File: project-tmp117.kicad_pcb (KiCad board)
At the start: 2 copper layers, 17 parts, among them J1 Conn_01x01_Pin, J2 Conn_01x01_Pin, J3 Conn_01x01_Pin, J4 Conn_01x01_Pin, J5 Conn_01x01_Pin, J7 SM04B-SRSS-TB(LF)(SN), J8 SM04B-SRSS-TB(LF)(SN), U1 TMP117AIDRVR

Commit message: First placement
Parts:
- moved R3 82.5 mm to (33.0, 20.0), turned to -90 degrees
- moved R4 80.7 mm to (36.0, 20.0), turned to -90 degrees
- moved R1 79.4 mm to (34.5, 20.0), turned to -90 degrees
- moved R2 77.4 mm to (37.5, 20.0), turned to -90 degrees
- moved J7 23.1 mm to (27.0, 26.0), turned to 0 degrees
- moved J8 14.6 mm to (27.0, 22.5)
- moved JP3 12.8 mm to (39.0, 29.0), turned to 90 degrees
- moved JP2 11.8 mm to (36.5, 29.0), turned to 90 degrees
- moved JP1 11.0 mm to (34.0, 29.0), turned to 90 degrees
- moved C2 10.5 mm to (40.5, 20.5), turned to 90 degrees
- moved J1 9.57 mm to (19.5, 20.2)
- moved J2 9.57 mm to (19.5, 24.2)
- moved J3 9.57 mm to (19.5, 22.2)
- moved J4 9.57 mm to (19.5, 26.2)
- moved J5 9.57 mm to (19.5, 28.2)
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
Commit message: Routing in progress
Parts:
- JP1: value 0x49 -> 49
- JP2: value 0x4A -> 4A
- JP3: value 0x4B -> 4B
- moved U1 9.50 mm to (56.0, 24.2), turned to 90 degrees
- moved C1 9.25 mm to (54.0, 24.2), turned to -90 degrees
- moved R2 5.51 mm to (34.0, 24.2)
- moved R4 5.51 mm to (32.5, 24.2)
- moved J2 2.06 mm to (20.0, 22.2)
- moved J3 2.06 mm to (20.0, 24.2)
- moved JP1 1.52 mm to (35.5, 29.2)
- moved JP2 1.52 mm to (38.0, 29.2)
- moved JP3 1.52 mm to (40.5, 29.2)
- moved C2 0.90 mm to (40.0, 19.8)
- moved J1 0.50 mm to (20.0, 20.2)
- moved J4 0.50 mm to (20.0, 26.2)
- moved J5 0.50 mm to (20.0, 28.2)
- moved R1 0.25 mm to (34.5, 19.8)
- moved R3 0.25 mm to (33.0, 19.8)
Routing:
- net /INT: track 0.00 -> 66.7 mm, vias 0 -> 2
- net /SDA: track 0.00 -> 63.6 mm
- net /SCL: track 0.00 -> 42.0 mm
- net /ADD0: track 0.00 -> 21.6 mm
- net VCC: track 0.00 -> 2.84 mm
- net GND: track 0.00 -> 1.02 mm, vias 0 -> 1
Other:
- board outline added: 40 x 14 mm

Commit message: Add a jumper for address 0x48
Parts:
- removed R3: 10k, Resistor_SMD:R_0603_1608Metric
- added JP4: 48, Jumper:SolderJumper-2_P1.3mm_Open_RoundedPad1.0x1.5mm, F.Cu at (33.0, 29.2)
- moved R1 0.50 mm to (34.0, 19.8), turned to 90 degrees
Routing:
- net /ADD0: track 21.6 -> 31.6 mm

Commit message: Remove the ALERT pull-up
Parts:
- removed R1: 10k, Resistor_SMD:R_0603_1608Metric
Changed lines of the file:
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@@
-		)
-	)
-	(footprint "Resistor_SMD:R_0603_1608Metric"
-		(layer "F.Cu")
-		(at 34 19.75 90)
-		(descr "Resistor SMD 0603 (1608 Metric), square (rectangular) end terminal, IPC_7351 nominal, (Body size source: IPC-SM-782 page 72, https://www.pcb-3d.com/wordpress/wp-content/uploads/ipc-sm-782a_amendment_1_and_2.pdf), generated with kicad-footprint-generator")
-		(tags "resistor")
-		(property "Reference" "R1"
-			(at 0 -1.43 270)
-			(layer "F.SilkS")
-			(hide yes)
-			(effects
-				(font
-					(size 1 1)
-					(thickness 0.15)
-				)
-			)
-		)
-		(property "Value" "10k"
-			(at 0 1.43 270)
-			(layer "F.Fab")
-			(hide yes)
-			(effects
-				(font
-					(size 1 1)
-					(thickness 0.15)
-				)
-			)
-		)
-		(property "Footprint" "Resistor_SMD:R_0603_1608Metric"
-			(at 0 0 90)
-			(unlocked yes)
-			(layer "F.Fab")
-			(hide yes)
-			(effects
-				(font
-					(size 1.27 1.27)
-				)
-			)
-		)
-		(property "Datasheet" ""
-			(at 0 0 90)
-			(unlocked yes)
-			(layer "F.Fab")
-			(hide yes)
-			(effects
-				(font
-					(size 1.27 1.27)
-				)
-			)
-		)
-		(property "Description" "Resistor"
-			(at 0 0 90)
-			(unlocked yes)
-			(layer "F.Fab")
-			(hide yes)
-			(effects
-				(font
-					(size 1.27 1.27)
-				)
-			)
-		)
-		(property ki_fp_filters "R_*")
-		(sheetname "Root")
-		(sheetfile "project-tmp117.kicad_sch")
-		(attr smd)
-		(fp_line
-			(start -0.237258 -0.5225)
-			(end 0.237258 -0.5225)
-			(stroke
-				(width 0.12)
-				(type solid)
-			)
-			(layer "F.SilkS")
-		)
-		(fp_line
-			(start -0.237258 0.5225)
-			(end 0.237258 0.5225)
-			(stroke
-				(width 0.12)
-				(type solid)
-			)
-			(layer "F.SilkS")
-		)
-		(fp_line
-			(start 1.48 -0.73)
-			(end 1.48 0.73)
-			(stroke
-				(width 0.05)
-				(type solid)
-			)
-			(layer "F.CrtYd")
-		)
-		(fp_line
-			(start -1.48 -0.73)
-			(end 1.48 -0.73)
-			(stroke
-				(width 0.05)
-				(type solid)
-			)
-			(layer "F.CrtYd")
-		)
-		(fp_line
-			(start 1.48 0.73)
-			(end -1.48 0.73)
-			(stroke
-				(width 0.05)
-				(type solid)
-			)
-			(layer "F.CrtYd")
-		)
-		(fp_line
-			(start -1.48 0.73)
-			(end -1.48 -0.73)
-			(stroke
-				(width 0.05)
-				(type solid)
-			)
-			(layer "F.CrtYd")
-		)
-		(fp_line
-			(start 0.8 -0.4125)
-			(end 0.8 0.4125)
-			(stroke
-				(width 0.1)
-				(type solid)
-			)
-			(layer "F.Fab")
-		)
-		(fp_line
-			(start -0.8 -0.4125)
-			(end 0.8 -0.4125)
-			(stroke
-				(width 0.1)
-				(type solid)
-			)
-			(layer "F.Fab")
-		)
-		(fp_line
-			(start 0.8 0.4125)
-			(end -0.8 0.4125)
-			(stroke
-				(width 0.1)
-				(type solid)
-			)
-			(layer "F.Fab")
-		)
-		(fp_line
-			(start -0.8 0.4125)
-			(end -0.8 -0.4125)
-			(stroke
-				(width 0.1)
-				(type solid)
-			)
-			(layer "F.Fab")
-		)
-		(fp_text user "${REFERENCE}"
-			(at 0 0 270)
-			(layer "F.Fab")
-			(effects
-				(font
-					(size 0.4 0.4)
-					(thickness 0.06)
-				)
-			)
-		)
-		(pad "1" smd roundrect
-			(at -0.825 0 90)
-			(size 0.8 0.95)
-			(layers "F.Cu" "F.Paste" "F.Mask")
-			(roundrect_rratio 0.25)
-			(net 2 "VCC")
-			(pintype "passive")
-		)
-		(pad "2" smd roundrect
-			(at 0.825 0 90)
-			(size 0.8 0.95)
-			(layers "F.Cu" "F.Paste" "F.Mask")
-			(roundrect_rratio 0.25)
-			(net 5 "/INT")
-			(pintype "passive")
-		)
-		(model "${KICAD8_3DMODEL_DIR}/Resistor_SMD.3dshapes/R_0603_1608Metric.wrl"
-			(offset
-				(xyz 0 0 0)
-			)
-			(scale
-				(xyz 1 1 1)
-			)
-			(rotate
-				(xyz 0 0 0)
-			)
 		)
 	)

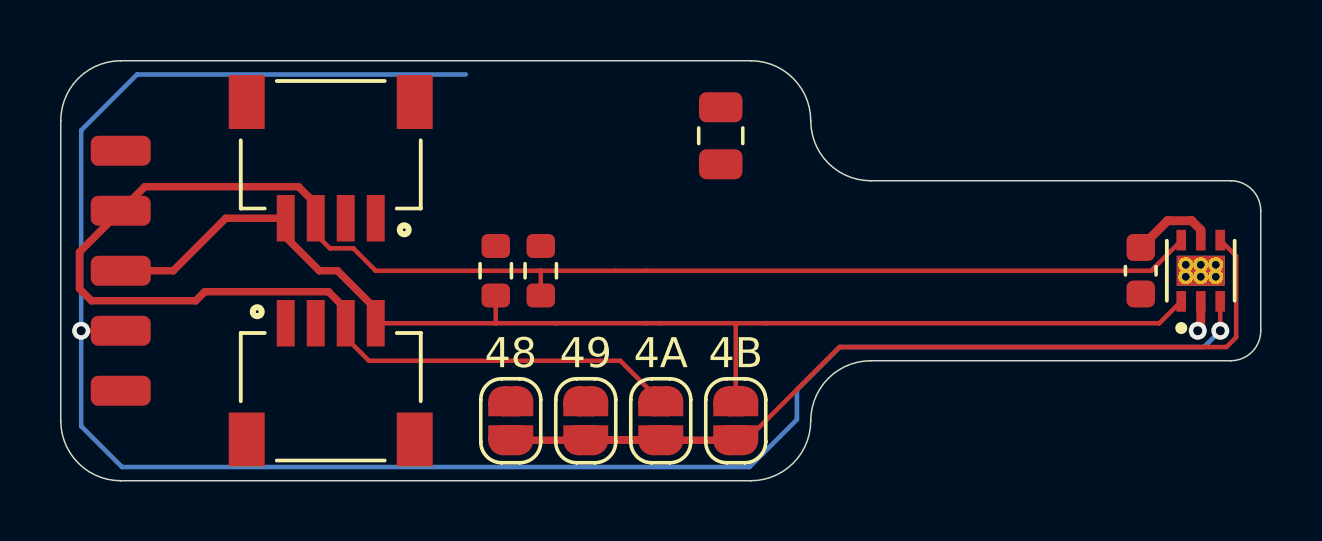
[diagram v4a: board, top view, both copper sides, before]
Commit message: First routing ready
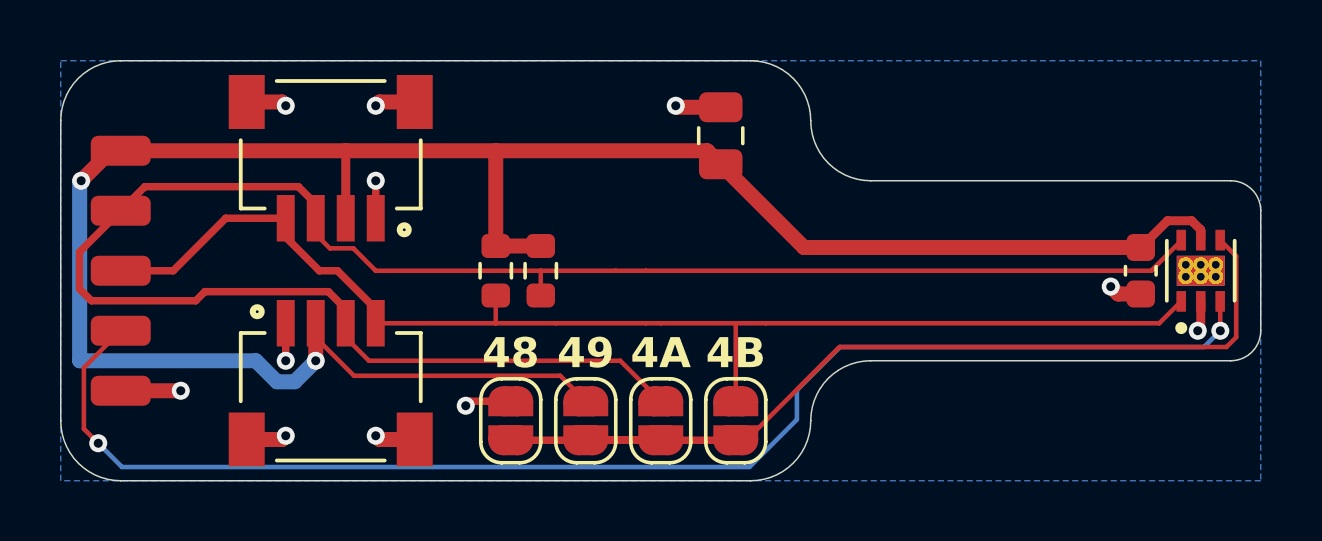
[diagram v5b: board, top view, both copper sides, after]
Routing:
- net VCC: track 2.84 -> 72.9 mm, vias 0 -> 2
- net /INT: track 66.7 -> 45.6 mm
- net GND: track 1.02 -> 15.1 mm, vias 1 -> 11
- added copper zone on B.Cu, net GND
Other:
- board text added: "François Gervais 2 avril 2024"

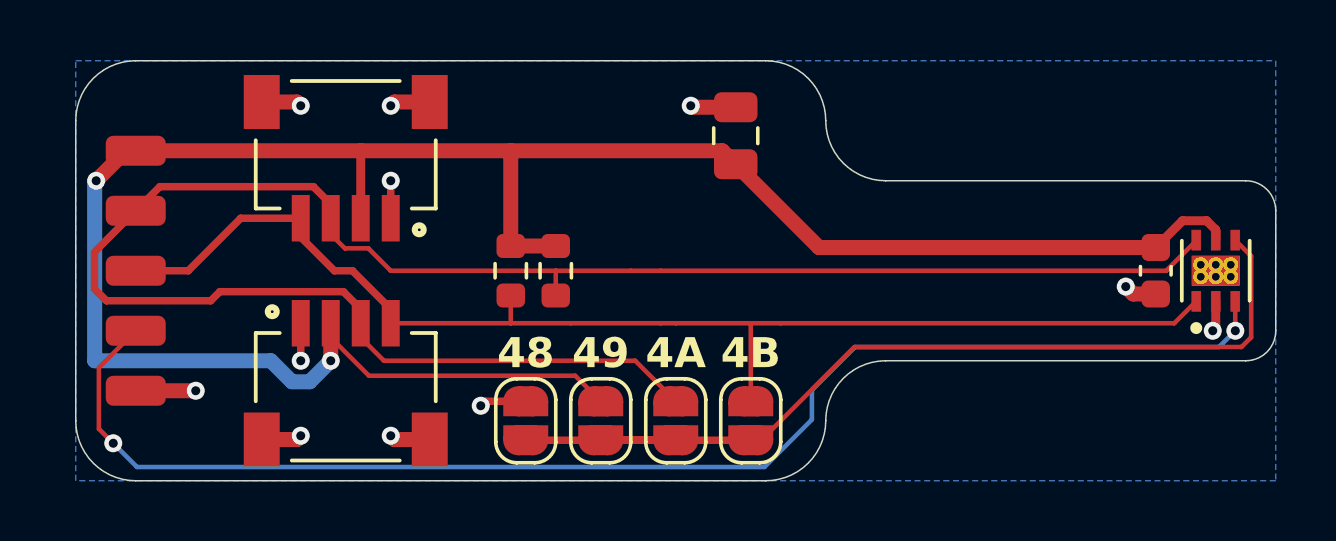
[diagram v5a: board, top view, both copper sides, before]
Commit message: Add header silkscreen
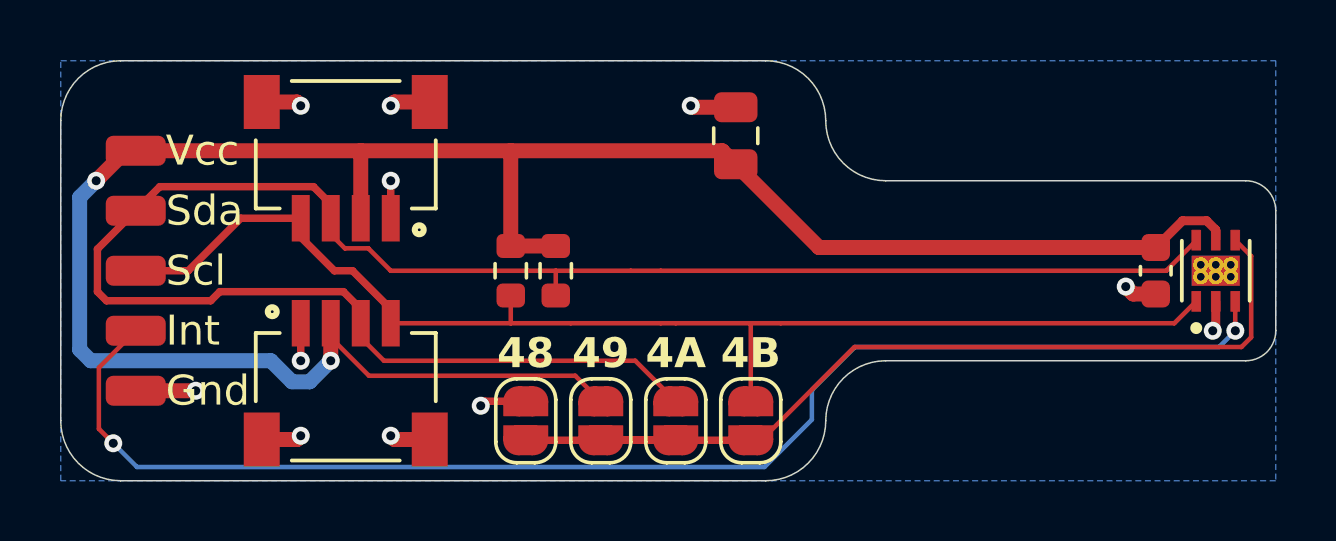
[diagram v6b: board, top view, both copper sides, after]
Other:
- board size 40 x 14 mm -> 40.5 x 14 mm
- board text added: "Gnd"
- board text added: "Int"
- board text added: "Scl"
- board text added: "Sda"
- board text added: "Vcc"
